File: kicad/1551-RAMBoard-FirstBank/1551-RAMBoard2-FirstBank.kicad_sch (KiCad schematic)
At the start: 12 parts, among them J1 Conn_01x02_Male, U1 27C512, U2 74LS139, U3 KM62256CLP, U4_SOCKET1 27128

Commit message: first attempt
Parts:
- removed J1: Conn_01x02_Male, Connector_PinHeader_2.54mm:PinHeader_1x02_P2.54mm_Vertical, symbol Connector:Conn_01x02_Male
- removed R14: 10K, Resistor_THT:R_Axial_DIN0207_L6.3mm_D2.5mm_P7.62mm_Horizontal, symbol Device:R
- removed RAM_A13: RAM_A13, Connector_PinHeader_2.54mm:PinHeader_1x02_P2.54mm_Vertical, symbol Jumper:Jumper_2_Open
- removed RAM_A14: RAM_A14, Connector_PinHeader_2.54mm:PinHeader_1x02_P2.54mm_Vertical, symbol Jumper:Jumper_2_Open
- removed ROM_A14: ROM_A14, Connector_PinHeader_2.54mm:PinHeader_1x02_P2.54mm_Vertical, symbol Jumper:Jumper_2_Open
- removed ROM_A15: ROM_A15, Connector_PinHeader_2.54mm:PinHeader_1x02_P2.54mm_Vertical, symbol Jumper:Jumper_2_Open
- added J1: Conn_01x02_Pin, Connector_PinHeader_2.54mm:PinHeader_1x02_P2.54mm_Vertical, symbol Connector:Conn_01x02_Pin
- added J2: Conn_01x03_Pin, Connector_PinHeader_2.54mm:PinHeader_1x03_P2.54mm_Vertical, symbol Connector:Conn_01x03_Pin
- added RAM_A13, RAM_A14: SolderJumper_2_Bridged, Jumper:SolderJumper-2_P1.3mm_Bridged_RoundedPad1.0x1.5mm, symbol Jumper:SolderJumper_2_Bridged
- added U4: 74LS00, Package_DIP:DIP-14_W7.62mm_Socket_LongPads, symbol 74xx:74LS00
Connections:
- net A14: now also U1.27 (A14), J2.2 (Pin_2)
- net GND: now also J1.2 (Pin_2), RAM_A13.1 (A), RAM_A14.1 (A), U4.7 (GND)
- net R/~{W}: now also J2.1 (Pin_1)
- net VCC: now also U4.10, U4.12, U4.13, U4.14 (VCC), U4.4, U4.5, U4.9
- net ~{A15}: now also U4.3; no longer U4_SOCKET1.22 (~{OE})
- net at R15.2, U1.1 (A15): now also J1.1 (Pin_1)
- net at U3.1 (A14): now also RAM_A14.2 (B)
- net at U3.26 (A13): now also RAM_A13.2 (B)
- new net A15: J2.3 (Pin_3), U4.1, U4.2
- no-connect marks 8 -> 12
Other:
- note added: "J1: - switch chooses ROM from 32K half of 27C512 closed = bottom half open = top half"
- note added: "J1: - switch chooses ROM from 32K half of 27C512: closed = bottom half, open = top half - RAM_A13 and RAM_A14 - close to use only 8K of RAM - RAM_A13 and RAM_A14 - open and connect jumper pins 2 (chip pins 1 and 26) to ??? port (???) to control which 8K bank is visible in $8000-$9FFF"
- note added: "J2: - A14 from CPU (U2) pin 21 or U7 pin 7 - A15 from CPU (U2) pin 22 or U7 pin 6 - R/~{W} from onboard RAM (U5) pin 21 or or gate array (U6) (pin 18) or U5 pin 19"
- note added: "unused gates"
- note removed: "- ROM_A14 - if closed, then R14 can be omitted and $A000-$FFFF is ROM (space for track cache buffer ROM code) - ROM_A14 - if open, then install R14 and a switch between jumper pin 2 (chip 27) and GND chooses ROM (1 of 4) - ROM_A15 - close for 27E257 or only upper half 32K of 27C512 - ROM_A15 - if open, then install R15 and a switch between jumper pin 2 (chip 1) and GND chooses ROM - RAM_A13 and R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"
- note removed: "J1: - A14 from CPU (U3) pin 24 - R/~{W} from onboard RAM (U5) pin 21 or gate array (U10) (pin 29 or 31 - check connection) or a via near R14"
- note removed: "optional"

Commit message: first try
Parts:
- removed H1: MountingHole, MountingHole:MountingHole_2.5mm, symbol Mechanical:MountingHole
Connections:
- net VPP: no longer names the net of U4_SOCKET1.1 (VPP)
- no-connect marks 12 -> 13
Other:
- note added: "J2: - A14 from CPU (U2) pin 21 or U7 pin 7 - A15 from CPU (U2) pin 22 or U7 pin 6 - R/~{W} from onboard RAM (U5) pin 21 or or gate array (U6) pin 31(?) or U3 pin 19(?)"
- note removed: "J2: - A14 from CPU (U2) pin 21 or U7 pin 7 - A15 from CPU (U2) pin 22 or U7 pin 6 - R/~{W} from onboard RAM (U5) pin 21 or or gate array (U6) (pin 18) or U5 pin 19"
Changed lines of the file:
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@@
 		)
 	)
-	(text "J2:\n- A14 from CPU (U2) pin 21 or U7 pin 7\n- A15 from CPU (U2) pin 22 or U7 pin 6\n- R/~{W} from onboard RAM (U5) pin 21 or\n  or gate array (U6) (pin 18)\n  or U5 pin 19"
+	(text "J2:\n- A14 from CPU (U2) pin 21 or U7 pin 7\n- A15 from CPU (U2) pin 22 or U7 pin 6\n- R/~{W} from onboard RAM (U5) pin 21 or\n  or gate array (U6) pin 31(?)\n  or U3 pin 19(?)"
 		(exclude_from_sim no)
 		(at 20.32 146.05 0)
@@
 	)
 	(no_connect
+		(at 113.03 97.79)
+	)
+	(no_connect
 		(at 135.89 139.7)
 	)
@@
 	(label "A5"
 		(at 113.03 69.85 180)
-		(effects
-			(font
-				(size 1.27 1.27)
-			)
-			(justify right bottom)
-		)
-	)
-	(label "VPP"
-		(at 113.03 97.79 180)
 		(effects
 			(font
@@
 					(unit 1)
 				)
-			)
-		)
-	)
-	(symbol
-		(lib_id "Mechanical:MountingHole")
-		(at 218.44 46.99 0)
-		(unit 1)
-		(exclude_from_sim no)
-		(in_bom yes)
-		(on_board yes)
-		(dnp no)
-		(fields_autoplaced yes)
-		(property "Reference" "H1"
-			(at 220.98 45.7199 0)
-			(effects
-				(font
-					(size 1.27 1.27)
-				)
-				(justify left)
-			)
-		)
-		(property "Value" "MountingHole"
-			(at 220.98 48.2599 0)
-			(effects
-				(font
-					(size 1.27 1.27)
-				)
-				(justify left)
-			)
-		)
-		(property "Footprint" "MountingHole:MountingHole_2.5mm"
-			(at 218.44 46.99 0)
-			(effects
-				(font
-					(size 1.27 1.27)
-				)
-				(hide yes)
-			)
-		)
-		(property "Datasheet" "~"
-			(at 218.44 46.99 0)
-			(effects
-				(font
-					(size 1.27 1.27)
-				)
-				(hide yes)
-			)
-		)
-		(property "Description" ""
-			(at 218.44 46.99 0)
-			(effects
-				(font
-					(size 1.27 1.27)
-				)
-			)
-		)
-		(instances
-			(project ""
-				(path "/f31d4332-8c61-492c-802c-a2a15cf9ccb2"
-					(reference "H1")
-					(unit 1)
-				)

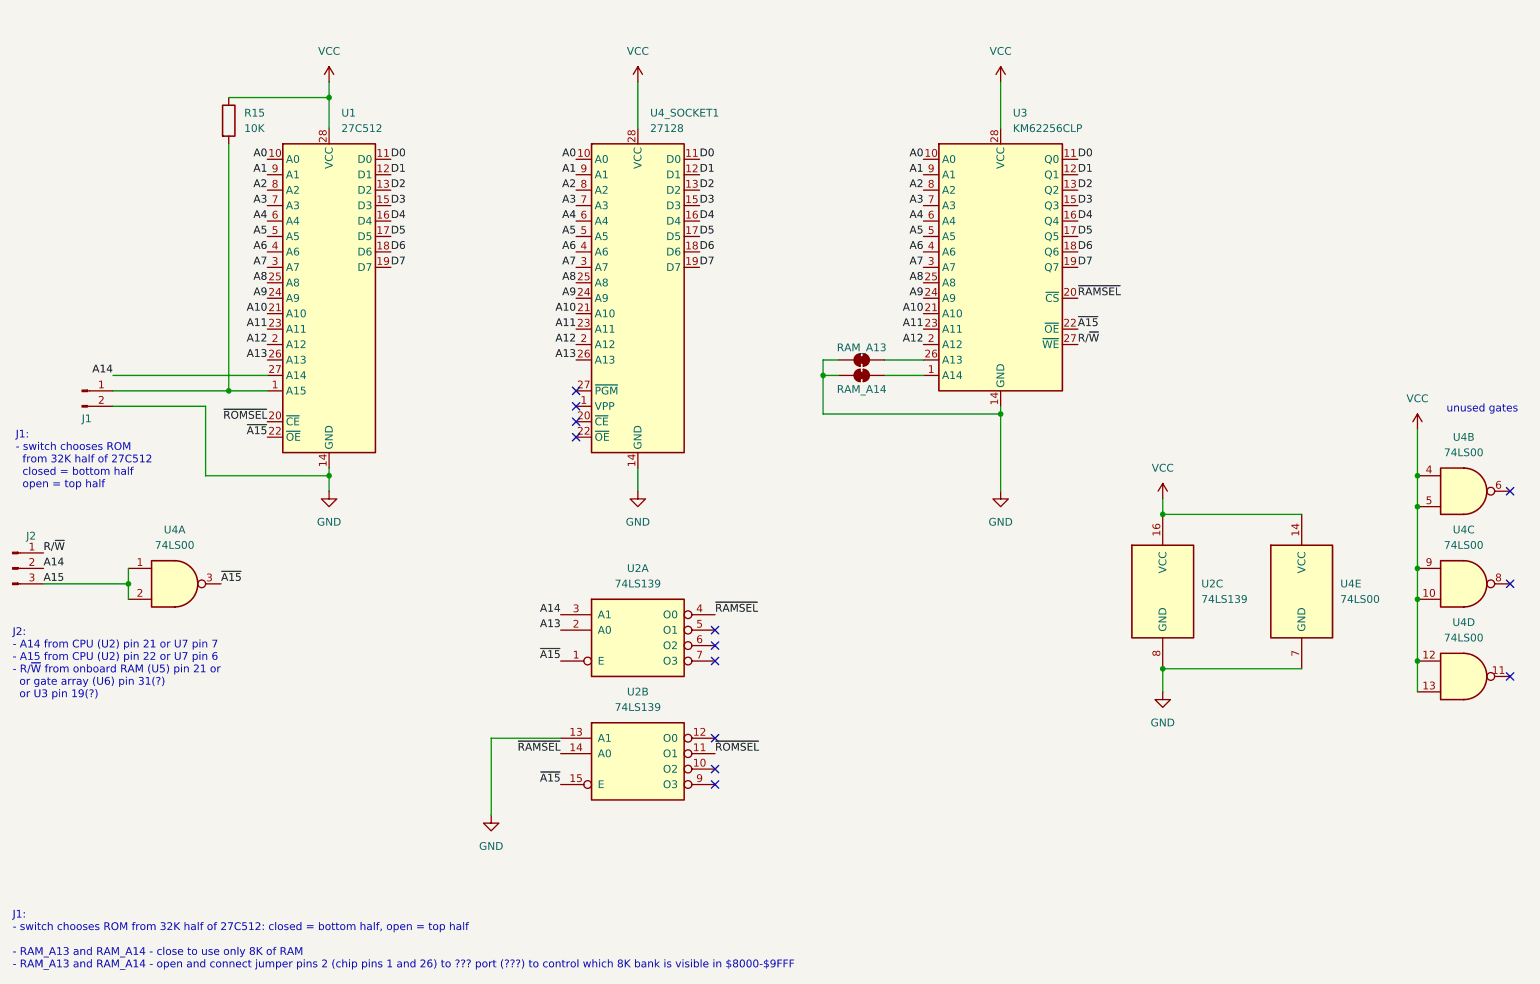
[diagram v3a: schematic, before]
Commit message: final touches, support for 6264 (8K) and 62256 (32K)
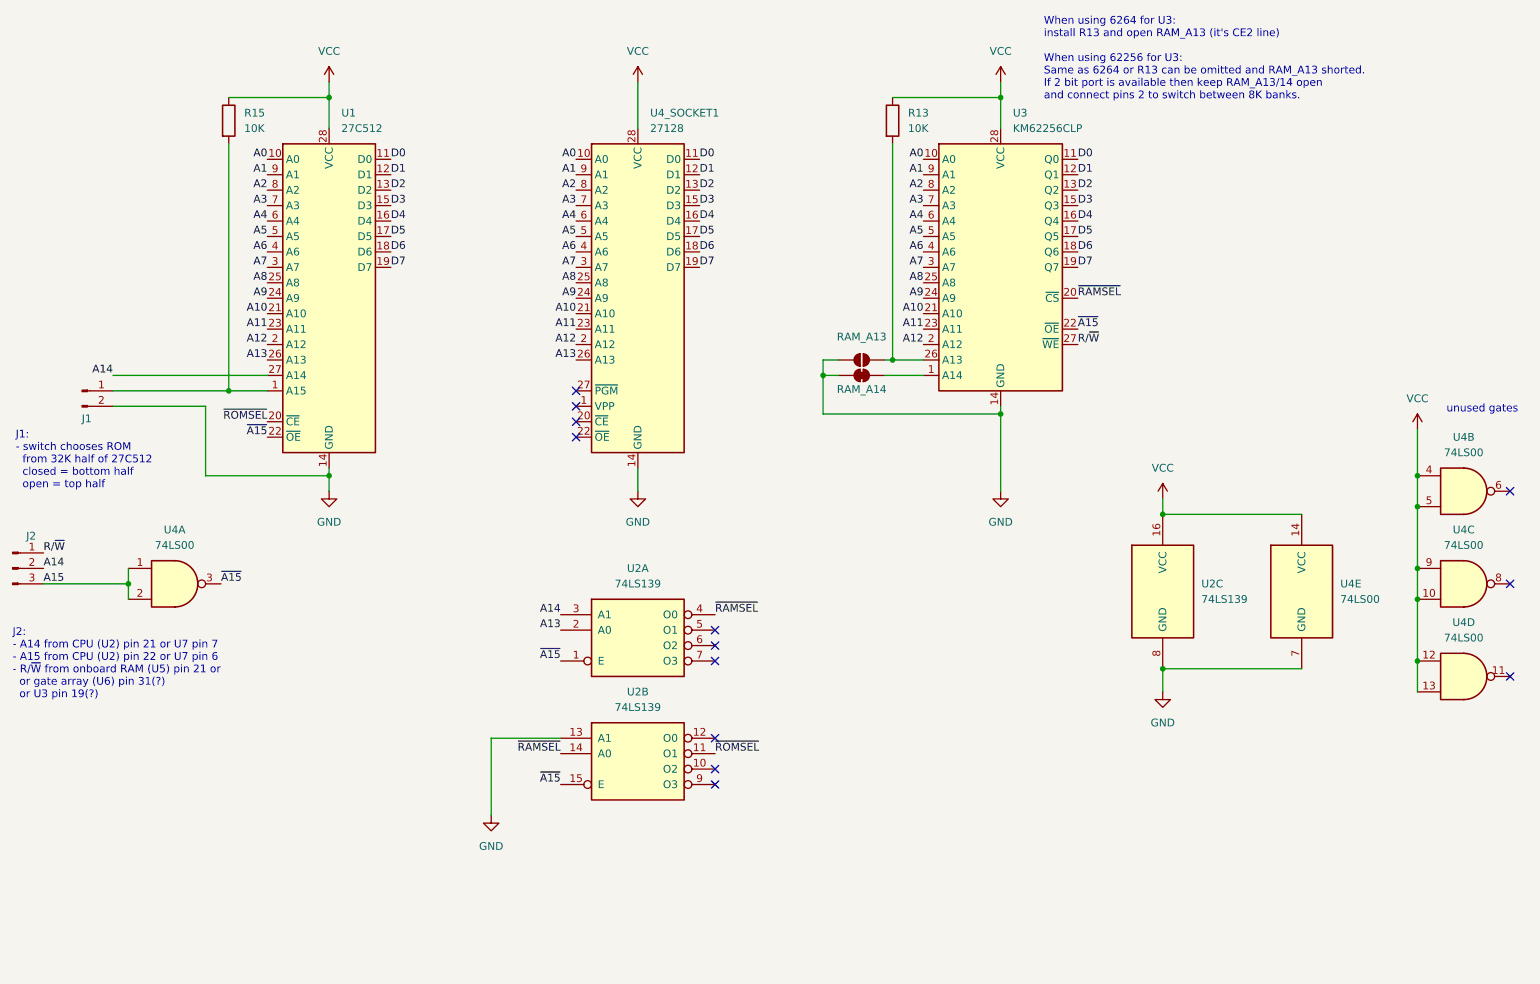
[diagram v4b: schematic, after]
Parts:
- removed RAM_A13: SolderJumper_2_Bridged, Jumper:SolderJumper-2_P1.3mm_Bridged_RoundedPad1.0x1.5mm, symbol Jumper:SolderJumper_2_Bridged
- added R13: 10K, Resistor_THT:R_Axial_DIN0207_L6.3mm_D2.5mm_P7.62mm_Horizontal, symbol Device:R
- added RAM_A13: SolderJumper_2_Open, Jumper:SolderJumper-2_P1.3mm_Open_RoundedPad1.0x1.5mm, symbol Jumper:SolderJumper_2_Open
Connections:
- net GND: now also RAM_A13.1 (A)
- net VCC: now also R13.1
- net at U3.26 (A13): now also R13.2, RAM_A13.2 (B)
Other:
- note added: "When using 6264 for U3: install R13 and open RAM_A13 (it's CE2 line) When using 62256 for U3: Same as 6264 or R13 can be omitted and RAM_A13 shorted. If 2 bit port is available then keep RAM_A13/14 open and connect pins 2 to switch between 8K banks."
- note removed: "J1: - switch chooses ROM from 32K half of 27C512: closed = bottom half, open = top half - RAM_A13 and RAM_A14 - close to use only 8K of RAM - RAM_A13 and RAM_A14 - open and connect jumper pins 2 (chip pins 1 and 26) to ??? port (???) to control which 8K bank is visible in $8000-$9FFF"
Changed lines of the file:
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@@
 		(comment 2 "1551 RAM and ROM expansion")
 	)
-	(text "J1:\n- switch chooses ROM from 32K half of 27C512: closed = bottom half, open = top half\n\n- RAM_A13 and RAM_A14 - close to use only 8K of RAM\n- RAM_A13 and RAM_A14 - open and connect jumper pins 2 (chip pins 1 and 26) to ??? port (???) to control which 8K bank is visible in $8000-$9FFF\n"
+	(text "When using 6264 for U3:\ninstall R13 and open RAM_A13 (it's CE2 line)\n\nWhen using 62256 for U3:\nSame as 6264 or R13 can be omitted and RAM_A13 shorted.\nIf 2 bit port is available then keep RAM_A13/14 open\nand connect pins 2 to switch between 8K banks."
 		(exclude_from_sim no)
-		(at 20.32 190.5 0)
+		(at 189.992 40.64 0)
 		(effects
 			(font
 				(size 1.27 1.27)
 			)
-			(justify left bottom)
+			(justify left)
 		)
 	)
@@
 	)
 	(junction
+		(at 165.1 90.17)
+		(diameter 0)
+		(color 0 0 0 0)
+	)
+	(junction
 		(at 251.46 114.3)
 		(diameter 0)
@@
 	)
 	(junction
+		(at 182.88 46.99)
+		(diameter 0)
+		(color 0 0 0 0)
+	)
+	(junction
 		(at 251.46 129.54)
 		(diameter 0)
@@
 	(wire
 		(pts
+			(xy 165.1 46.99) (xy 182.88 46.99)
+		)
+		(stroke
+			(width 0)
+			(type default)
+		)
+	)
+	(wire
+		(pts
+			(xy 165.1 54.61) (xy 165.1 90.17)
+		)
+		(stroke
+			(width 0)
+			(type default)
+		)
+	)
+	(wire
+		(pts
 			(xy 182.88 97.79) (xy 182.88 99.06)
 		)
@@
 	(wire
 		(pts
+			(xy 182.88 46.99) (xy 182.88 52.07)
+		)
+		(stroke
+			(width 0)
+			(type default)
+		)
+	)
+	(wire
+		(pts
 			(xy 251.46 139.7) (xy 251.46 144.78)
 		)
@@
 	(wire
 		(pts
+			(xy 165.1 90.17) (xy 170.18 90.17)
+		)
+		(stroke
+			(width 0)
+			(type default)
+		)
+	)
+	(wire
+		(pts
 			(xy 251.46 109.22) (xy 251.46 114.3)
 		)
@@
 	(wire
 		(pts
-			(xy 182.88 44.45) (xy 182.88 52.07)
+			(xy 182.88 44.45) (xy 182.88 46.99)
 		)
 		(stroke
@@
 	(wire
 		(pts
-			(xy 163.83 90.17) (xy 170.18 90.17)
+			(xy 163.83 90.17) (xy 165.1 90.17)
 		)
 		(stroke
@@
 	)
 	(symbol
+		(lib_id "Jumper:SolderJumper_2_Open")
+		(at 160.02 90.17 0)
+		(unit 1)
+		(exclude_from_sim no)
+		(in_bom no)
+		(on_board yes)
+		(dnp no)
+		(fields_autoplaced yes)
+		(property "Reference" "RAM_A13"
+			(at 160.02 86.36 0)
+			(effects
+				(font
+					(size 1.27 1.27)
+				)
+			)
+		)
+		(property "Value" "SolderJumper_2_Open"
+			(at 160.02 86.36 0)
+			(effects
+				(font
+					(size 1.27 1.27)
+				)
+				(hide yes)
+			)
+		)
+		(property "Footprint" "Jumper:SolderJumper-2_P1.3mm_Open_RoundedPad1.0x1.5mm"
+			(at 160.02 90.17 0)
+			(effects
+				(font
+					(size 1.27 1.27)
+				)
+				(hide yes)
+			)
+		)
+		(property "Datasheet" "~"
+			(at 160.02 90.17 0)
+			(effects
+				(font
+					(size 1.27 1.27)
+				)
+				(hide yes)
+			)
+		)
+		(property "Description" "Solder Jumper, 2-pole, open"
+			(at 160.02 90.17 0)
+			(effects
+				(font
+					(size 1.27 1.27)
+				)
+				(hide yes)
+			)
+		)
+		(pin "1"
+		)
+		(pin "2"
+		)
+		(instances
+			(project ""
+				(path "/f31d4332-8c61-492c-802c-a2a15cf9ccb2"
+					(reference "RAM_A13")
+					(unit 1)
+				)
+			)
+		)
+	)
+	(symbol
 		(lib_id "power:GND")
 		(at 209.55 144.78 0)
@@
 	)
 	(symbol
+		(lib_id "Device:R")
+		(at 165.1 50.8 0)
+		(unit 1)
+		(exclude_from_sim no)
+		(in_bom yes)
+		(on_board yes)
+		(dnp no)
+		(fields_autoplaced yes)
+		(property "Reference" "R13"
+			(at 167.64 49.5299 0)
+			(effects
+				(font
+					(size 1.27 1.27)
+				)
+				(justify left)
+			)
+		)
+		(property "Value" "10K"
+			(at 167.64 52.0699 0)
+			(effects
+				(font
+					(size 1.27 1.27)
+				)
+				(justify left)
+			)
+		)
+		(property "Footprint" "Resistor_THT:R_Axial_DIN0207_L6.3mm_D2.5mm_P7.62mm_Horizontal"
+			(at 163.322 50.8 90)
+			(effects
+				(font
+					(size 1.27 1.27)
+				)
+				(hide yes)
+			)
+		)
+		(property "Datasheet" "~"
+			(at 165.1 50.8 0)
+			(effects
+				(font
+					(size 1.27 1.27)
+				)
+				(hide yes)
+			)
+		)
+		(property "Description" ""
+			(at 165.1 50.8 0)
+			(effects
+				(font
+					(size 1.27 1.27)
+				)
+			)
+		)
+		(pin "1"
+		)
+		(pin "2"
+		)
+		(instances
+			(project "1551-RAMBoard2-FirstBank"
+				(path "/f31d4332-8c61-492c-802c-a2a15cf9ccb2"
+					(reference "R13")
+					(unit 1)
+				)
+			)
+		)
+	)
+	(symbol
 		(lib_id "power:GND")
 		(at 72.39 111.76 0)
@@
 					(unit 1)
 				)
-			)
-		)
-	)
-	(symbol
-		(lib_id "Jumper:SolderJumper_2_Bridged")
-		(at 160.02 90.17 0)
-		(unit 1)
-		(exclude_from_sim no)
-		(in_bom no)
-		(on_board yes)
-		(dnp no)
-		(property "Reference" "RAM_A13"
-			(at 160.02 88.138 0)
-			(effects
-				(font
-					(size 1.27 1.27)
-				)
-			)
-		)
-		(property "Value" "SolderJumper_2_Bridged"
-			(at 160.02 86.36 0)
-			(effects
-				(font
-					(size 1.27 1.27)
-				)
-				(hide yes)
-			)
-		)
-		(property "Footprint" "Jumper:SolderJumper-2_P1.3mm_Bridged_RoundedPad1.0x1.5mm"
-			(at 160.02 90.17 0)
-			(effects
-				(font
-					(size 1.27 1.27)
-				)
-				(hide yes)
-			)
-		)
-		(property "Datasheet" "~"
-			(at 160.02 90.17 0)
-			(effects
-				(font
-					(size 1.27 1.27)
-				)
-				(hide yes)
-			)
-		)
-		(property "Description" "Solder Jumper, 2-pole, closed/bridged"
-			(at 160.02 90.17 0)
-			(effects
-				(font
-					(size 1.27 1.27)
-				)
-				(hide yes)
-			)
-		)
-		(pin "1"
-		)
-		(pin "2"
-		)
-		(instances
-			(project ""
-				(path "/f31d4332-8c61-492c-802c-a2a15cf9ccb2"
-					(reference "RAM_A13")
-					(unit 1)
-				)

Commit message: updates after real hardware test, clarify R/W connection info
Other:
- note added: "J2: - A14 from CPU (U2) pin 21 or U7 pin 7 - A15 from CPU (U2) pin 22 or U7 pin 6 - R/~{W} from onboard RAM (U5) pin 21 or or U3 pin 19"
- note removed: "J2: - A14 from CPU (U2) pin 21 or U7 pin 7 - A15 from CPU (U2) pin 22 or U7 pin 6 - R/~{W} from onboard RAM (U5) pin 21 or or gate array (U6) pin 31(?) or U3 pin 19(?)"
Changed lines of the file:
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@@
 		)
 	)
-	(text "J2:\n- A14 from CPU (U2) pin 21 or U7 pin 7\n- A15 from CPU (U2) pin 22 or U7 pin 6\n- R/~{W} from onboard RAM (U5) pin 21 or\n  or gate array (U6) pin 31(?)\n  or U3 pin 19(?)"
+	(text "J2:\n- A14 from CPU (U2) pin 21 or U7 pin 7\n- A15 from CPU (U2) pin 22 or U7 pin 6\n- R/~{W} from onboard RAM (U5) pin 21 or\n  or U3 pin 19"
 		(exclude_from_sim no)
 		(at 20.32 146.05 0)
